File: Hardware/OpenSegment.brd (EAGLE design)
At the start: 35.6 x 38.1 mm, 53 parts, among them Q1 PNP, Q10 MMBT2222, Q11 MMBT2222, Q12 MMBT2222, Q2 PNP, Q3 PNP, Q4 PNP, Q5 PNP, Q6 PNP, Q7 PNP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

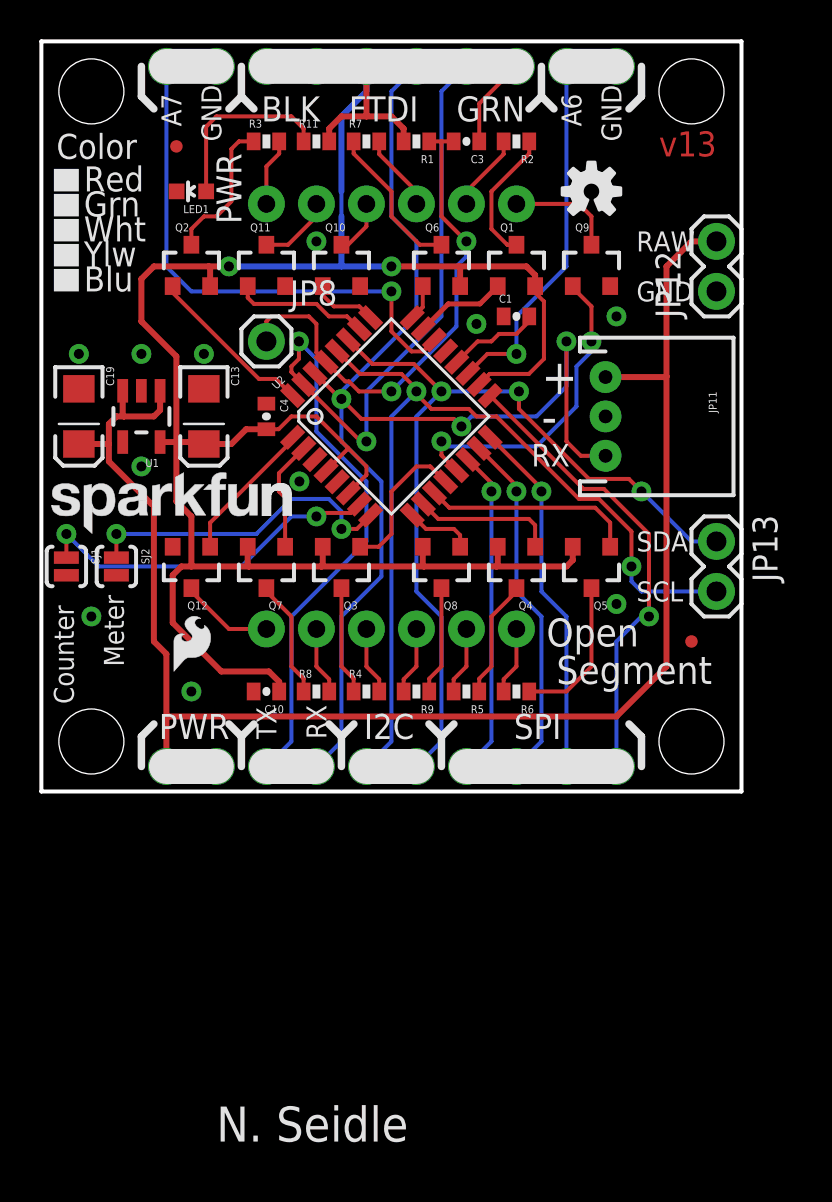
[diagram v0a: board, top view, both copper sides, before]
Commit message: Commit For Desk Change
Only doing this commit so I can work at the new QC desk
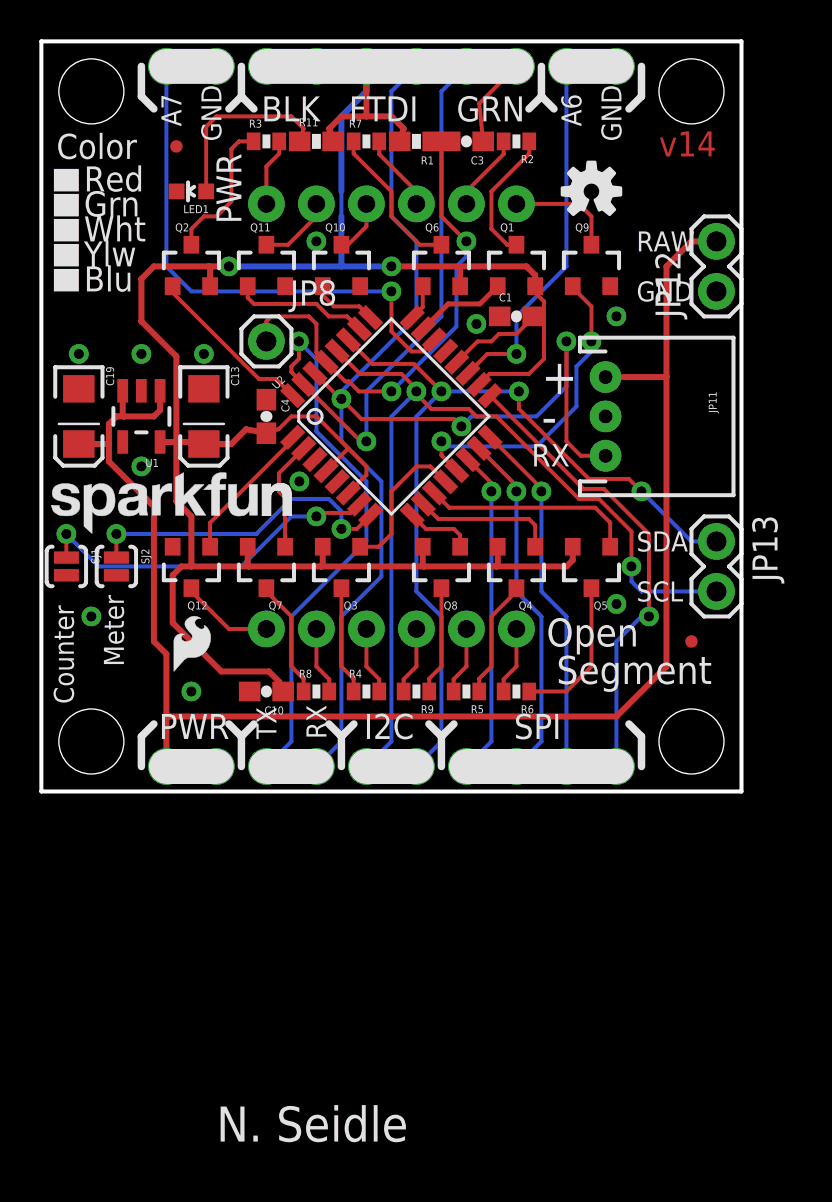
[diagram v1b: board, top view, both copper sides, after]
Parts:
- added FRAME1: FRAME-LETTER, SparkFun-Aesthetics:CREATIVE_COMMONS
- C1, C10, C3, C4: device SparkFun:0402-CAP -> SparkFun-Capacitors:0603-CAP
- R1, R11: device SparkFun:0402-RES -> SparkFun-Resistors:0603-RES
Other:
- board text added: "v14"
- board text removed: "v13"

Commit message: Cap/res changed, updated schematic
Changed cap/res to 0603 footprints
Updated SCH to fr-lttr  also updated to our current flag standards
Minor trace re-routing
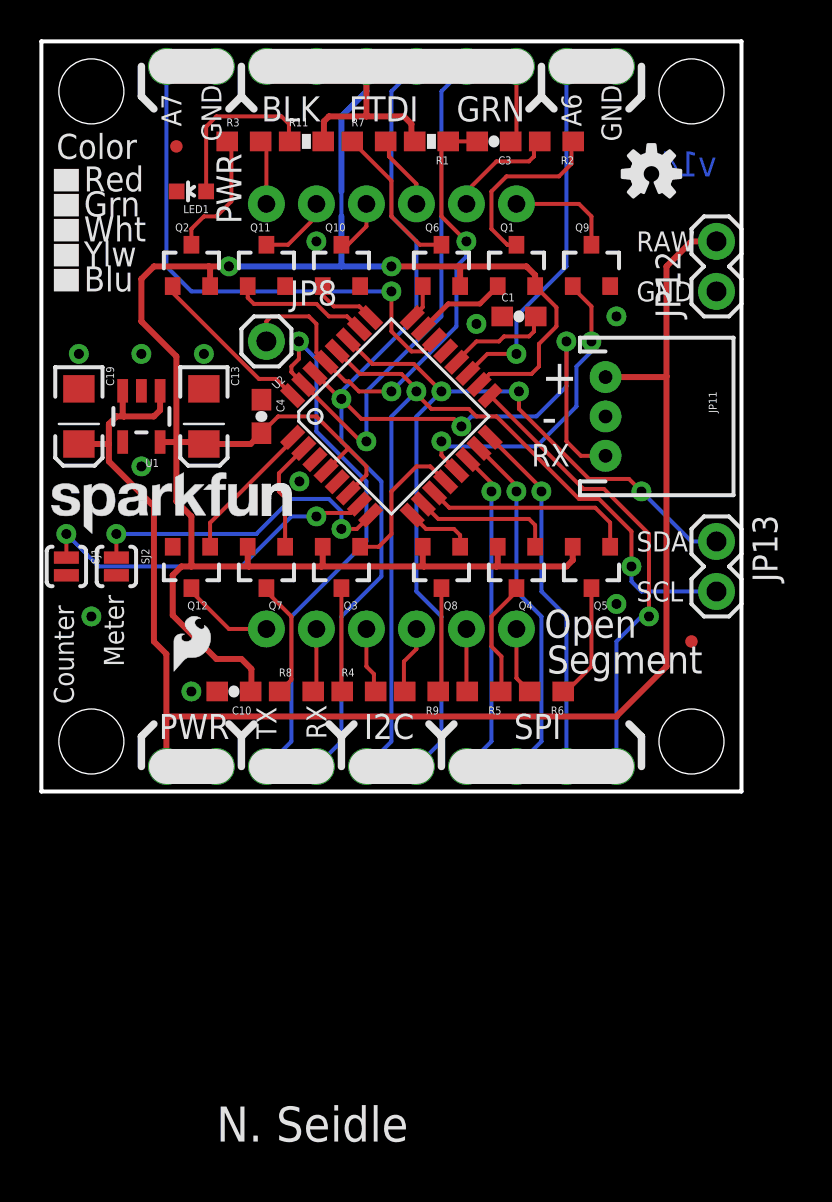
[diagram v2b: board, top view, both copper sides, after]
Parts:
- R2, R3, R4, R5, R6, R7, R8, R9: device SparkFun:0402-RES -> SparkFun-Resistors:0603
- moved U$4 3.18 mm to (13.2, 12.3)
- moved R2 2.03 mm to (8.38, 14.0)
- moved C10 1.65 mm to (-8.00, -14.0)
- moved R6 1.52 mm to (7.87, -14.0)
- moved C3 1.40 mm to (5.21, 14.0)
- moved R3 1.14 mm to (-7.49, 14.0)
- moved R8 1.02 mm to (-4.83, -14.0)
- moved R5 0.89 mm to (4.70, -14.0)
- moved R1 0.76 mm to (2.03, 14.0)
- moved R11 0.51 mm to (-4.32, 14.0)
- moved R4 0.38 mm to (-1.65, -14.0)
- moved C4 0.25 mm to (-6.60, 0.00)
- moved R9 0.25 mm to (1.52, -14.0)
- moved C1 0.13 mm to (6.48, 5.08)
- moved R7 0.13 mm to (-1.14, 14.0)
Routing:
- net N$1: track 6.84 -> 9.33 mm
- net SEGA: track 3.96 -> 5.68 mm
- net N$7: track 7.67 -> 5.94 mm
- net RST: track 25.5 -> 26.7 mm
- net N$4: track 7.37 -> 6.55 mm
- net N$3: track 4.60 -> 3.93 mm
- net VCC: track 115.9 -> 116.5 mm
- net N$38: track 9.39 -> 8.77 mm

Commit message: Desk Change
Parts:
- removed U$3: CREATIVE_COMMONS, SparkFun:CREATIVE_COMMONS
- FRAME1: value FRAME-LETTER -> FRAME-LEDGER
- LED1: device SparkFun:LED-0603 -> SparkFun-LED:LED-0603
- moved LED1 0.31 mm to (-10.5, 11.4)

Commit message: added regular fiducials
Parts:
- removed JP14, JP7: FIDUCIALUFIDUCIAL, SparkFun:MICRO-FIDUCIAL
- added FID1, FID2: FIDUCIAL1X2, SparkFun-Aesthetics:FIDUCIAL-1X2
